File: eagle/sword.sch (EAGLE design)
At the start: 4 parts, among them U1 TINY45-20-DIP

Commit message: major schematic fail...
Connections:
- new net N$1: J1.1, S1.P1
- net GND: no longer S1.P
- net VCC: no longer J1.1
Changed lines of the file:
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@@
 <?xml version="1.0" encoding="utf-8"?>
 <!DOCTYPE eagle SYSTEM "eagle.dtd">
-<eagle version="7.5.0">
+<eagle version="8.0.0">
 <drawing>
 <settings>
@@
 <pinref part="U1" gate="G$1" pin="VCC"/>
 <wire x1="45.72" y1="58.42" x2="40.64" y2="58.42" width="0.1524" layer="91"/>
-<pinref part="S1" gate="1" pin="S1"/>
-<pinref part="J1" gate="G$1" pin="1"/>
-<wire x1="40.64" y1="58.42" x2="33.02" y2="58.42" width="0.1524" layer="91"/>
 <wire x1="40.64" y1="58.42" x2="40.64" y2="66.04" width="0.1524" layer="91"/>
-<wire x1="40.64" y1="66.04" x2="40.64" y2="73.66" width="0.1524" layer="91"/>
 <wire x1="40.64" y1="66.04" x2="50.8" y2="66.04" width="0.1524" layer="91"/>
 <wire x1="50.8" y1="66.04" x2="50.8" y2="73.66" width="0.1524" layer="91"/>
 <label x="50.8" y="73.66" size="1.778" layer="95" rot="R90" xref="yes"/>
+<pinref part="S1" gate="1" pin="S1"/>
+<wire x1="33.02" y1="58.42" x2="40.64" y2="58.42" width="0.1524" layer="91"/>
 </segment>
 </net>
@@
 <segment>
 <pinref part="U1" gate="G$1" pin="GND"/>
-<pinref part="S1" gate="1" pin="P"/>
 <wire x1="45.72" y1="45.72" x2="40.64" y2="45.72" width="0.1524" layer="91"/>
-<wire x1="40.64" y1="45.72" x2="30.48" y2="45.72" width="0.1524" layer="91"/>
-<wire x1="30.48" y1="45.72" x2="30.48" y2="48.26" width="0.1524" layer="91"/>
 <pinref part="J2" gate="G$1" pin="1"/>
 <wire x1="40.64" y1="27.94" x2="40.64" y2="35.56" width="0.1524" layer="91"/>
@@
 </segment>
 </net>
+<net name="N$1" class="0">
+<segment>
+<pinref part="J1" gate="G$1" pin="1"/>
+<wire x1="40.64" y1="73.66" x2="40.64" y2="68.58" width="0.1524" layer="91"/>
+<wire x1="40.64" y1="68.58" x2="17.78" y2="68.58" width="0.1524" layer="91"/>
+<wire x1="17.78" y1="68.58" x2="17.78" y2="43.18" width="0.1524" layer="91"/>
+<wire x1="17.78" y1="43.18" x2="33.02" y2="43.18" width="0.1524" layer="91"/>
+<pinref part="S1" gate="1" pin="P1"/>
+<wire x1="33.02" y1="43.18" x2="33.02" y2="48.26" width="0.1524" layer="91"/>
+</segment>
+</net>

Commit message: added battery "connector"
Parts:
- added J3, J4: (no value), SparkFun-Connectors:M01PTH_LONGPAD
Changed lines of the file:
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@@
 <part name="J1" library="SparkFun-Connectors" deviceset="M01" device="PTH_LONGPAD"/>
 <part name="J2" library="SparkFun-Connectors" deviceset="M01" device="PTH_LONGPAD"/>
+<part name="J3" library="SparkFun-Connectors" deviceset="M01" device="PTH_LONGPAD"/>
+<part name="J4" library="SparkFun-Connectors" deviceset="M01" device="PTH_LONGPAD"/>
 </parts>
 <sheets>
@@
 <instance part="J1" gate="G$1" x="40.64" y="81.28" rot="R270"/>
 <instance part="J2" gate="G$1" x="40.64" y="20.32" rot="R90"/>
+<instance part="J3" gate="G$1" x="33.02" y="81.28" rot="R270"/>
+<instance part="J4" gate="G$1" x="33.02" y="20.32" rot="R90"/>
 </instances>
 <busses>

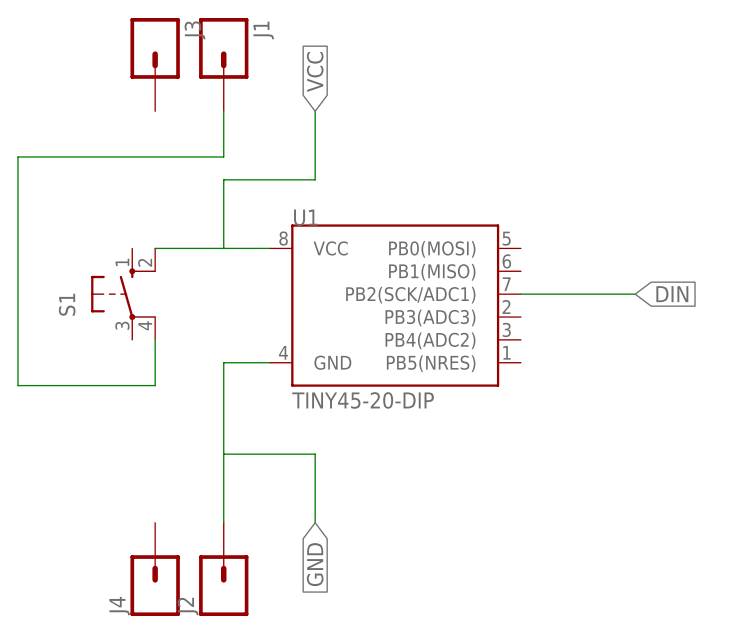
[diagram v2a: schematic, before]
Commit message: changed board to use a standard cr2032 socket
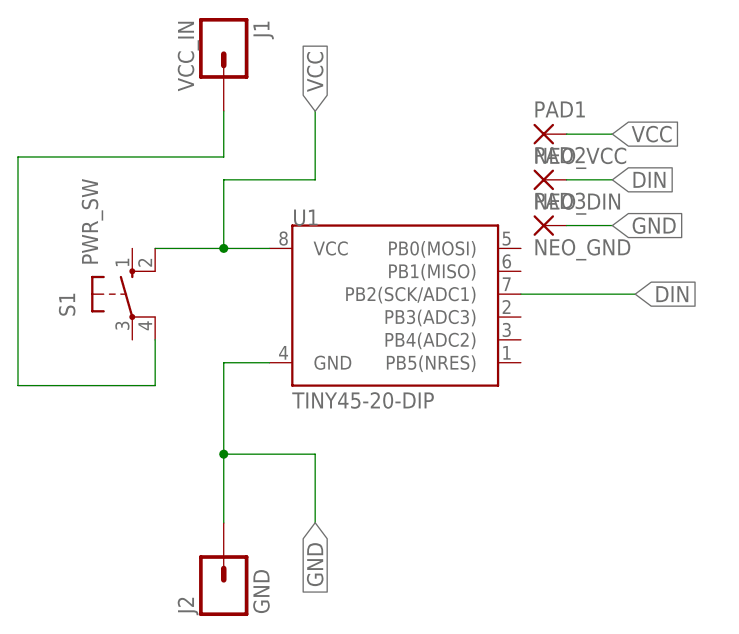
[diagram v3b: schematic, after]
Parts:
- removed J3, J4: (no value), SparkFun-Connectors:M01PTH_LONGPAD
- added PAD1: NEO_VCC, wirepad:SMD2
- added PAD2: NEO_DIN, wirepad:SMD2
- added PAD3: NEO_GND, wirepad:SMD2
- J1: value (none) -> VCC_IN
- J2: value (none) -> GND
- S1: value (none) -> PWR_SW
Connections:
- net N$1 renamed VCC_SW
- net DIN: now also PAD2.P
- net GND: now also PAD3.P
- net VCC: now also PAD1.P
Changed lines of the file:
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@@
 <parts>
 <part name="U1" library="SparkFun-DigitalIC" deviceset="ATTINY45" device="TINY45-20-DIP" value="TINY45-20-DIP"/>
-<part name="S1" library="switch-omron" deviceset="10-XX" device=""/>
-<part name="J1" library="SparkFun-Connectors" deviceset="M01" device="PTH_LONGPAD"/>
-<part name="J2" library="SparkFun-Connectors" deviceset="M01" device="PTH_LONGPAD"/>
-<part name="J3" library="SparkFun-Connectors" deviceset="M01" device="PTH_LONGPAD"/>
-<part name="J4" library="SparkFun-Connectors" deviceset="M01" device="PTH_LONGPAD"/>
+<part name="S1" library="switch-omron" deviceset="10-XX" device="" value="PWR_SW"/>
+<part name="J1" library="SparkFun-Connectors" deviceset="M01" device="PTH_LONGPAD" value="VCC_IN"/>
+<part name="J2" library="SparkFun-Connectors" deviceset="M01" device="PTH_LONGPAD" value="GND"/>
+<part name="PAD1" library="wirepad" deviceset="SMD2" device="" value="NEO_VCC"/>
+<part name="PAD2" library="wirepad" deviceset="SMD2" device="" value="NEO_DIN"/>
+<part name="PAD3" library="wirepad" deviceset="SMD2" device="" value="NEO_GND"/>
 </parts>
 <sheets>
@@
 <instance part="J1" gate="G$1" x="40.64" y="81.28" rot="R270"/>
 <instance part="J2" gate="G$1" x="40.64" y="20.32" rot="R90"/>
-<instance part="J3" gate="G$1" x="33.02" y="81.28" rot="R270"/>
-<instance part="J4" gate="G$1" x="33.02" y="20.32" rot="R90"/>
+<instance part="PAD1" gate="1" x="76.2" y="71.12"/>
+<instance part="PAD2" gate="1" x="76.2" y="66.04"/>
+<instance part="PAD3" gate="1" x="76.2" y="60.96"/>
 </instances>
 <busses>
@@
 <pinref part="S1" gate="1" pin="S1"/>
 <wire x1="33.02" y1="58.42" x2="40.64" y2="58.42" width="0.1524" layer="91"/>
+<junction x="40.64" y="58.42"/>
+</segment>
+<segment>
+<pinref part="PAD1" gate="1" pin="P"/>
+<wire x1="78.74" y1="71.12" x2="83.82" y2="71.12" width="0.1524" layer="91"/>
+<label x="83.82" y="71.12" size="1.778" layer="95" xref="yes"/>
 </segment>
 </net>
@@
 <wire x1="50.8" y1="35.56" x2="50.8" y2="27.94" width="0.1524" layer="91"/>
 <label x="50.8" y="27.94" size="1.778" layer="95" rot="R270" xref="yes"/>
+<junction x="40.64" y="35.56"/>
+</segment>
+<segment>
+<pinref part="PAD3" gate="1" pin="P"/>
+<wire x1="78.74" y1="60.96" x2="83.82" y2="60.96" width="0.1524" layer="91"/>
+<label x="83.82" y="60.96" size="1.778" layer="95" xref="yes"/>
 </segment>
 </net>
@@
 <label x="86.36" y="53.34" size="1.778" layer="95" xref="yes"/>
 </segment>
+<segment>
+<pinref part="PAD2" gate="1" pin="P"/>
+<wire x1="78.74" y1="66.04" x2="83.82" y2="66.04" width="0.1524" layer="91"/>
+<label x="83.82" y="66.04" size="1.778" layer="95" xref="yes"/>
+</segment>
 </net>
-<net name="N$1" class="0">
+<net name="VCC_SW" class="0">
 <segment>
 <pinref part="J1" gate="G$1" pin="1"/>
